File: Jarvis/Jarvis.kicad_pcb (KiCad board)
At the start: 2 copper layers, 34 x 65 mm, 121 parts, among them IC1 ADP1607, IC2 STM32F411CxUx, IC3 Si4460, IC4 MS5611-01BA03, IC5 MAX-8Q, IC6 MPU-9250, J1 PWR, J2 PYRO, J3 ARM, J4 EXT, P1 SWD_TC, P2 SMA, Q1 NFET, Q2 NFET, Q3 NFET, Q4 PFET, Q5 PFET, Q6 NFET, Q7 PFET, U1 MICROSD, Y1 26MHz, Y2 30MHz

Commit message: Schematic Complete
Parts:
- removed C22, C27, C30: 100nF, agg:0402-L
- removed C25: 1uF, agg:0603-L
- removed C33: 10nF, agg:0402-L
- removed J4: EXT, agg:SIL-254P-04
- removed R37: 1k, agg:0402-L
- removed REF**: Molex_PicoBlade_53261-0471, Connectors_Molex:Molex_PicoBlade_53261-0471
- added C19: 10nF, agg:0402-L, F.Cu at (241.0, 122.6)
- added C23: 100nF, agg:0402-L, F.Cu at (247.8, 116.4)
- added C26: 1uF, agg:0603-L, F.Cu at (217.8, 125.0)
- added C28: 100nF, agg:0402-L, F.Cu at (233.3, 130.3)
- added C29: 100nF, agg:0402-L, F.Cu at (218.4, 145.8)
- C11: value 8pF -> 100nF
- C13: value 100nF -> 8pF
- C14: value 4.7uF -> 100nF
- C15: value 10uF -> 4.7uF; footprint agg:0805 -> agg:0402-L
- C17: value 100nF -> 10uF; footprint agg:0402-L -> agg:0805
- IC2: value STM32F411CxUx -> MS5611-01BA03; footprint agg:QFN-48-EP-ST -> agg:MS5611
- IC3: value Si4460 -> STM32F411CxUx; footprint agg:QFN-20-EP-SI -> agg:QFN-48-EP-ST
- IC4: value MS5611-01BA03 -> Si4460; footprint agg:MS5611 -> agg:QFN-20-EP-SI; moved to F.Cu
- IC5: value MAX-8Q -> MPU-9250; footprint Library:MAX-7Q -> agg:QFN-24-MPU9250
- IC6: value MPU-9250 -> MAX-8Q; footprint agg:QFN-24-MPU9250 -> Library:MAX-7Q; moved to F.Cu
- J2: value PYRO -> ARM; footprint agg:S06B-PASK-2 -> agg:S03B-PASK-2
- J3: value ARM -> PYRO; footprint agg:S02B-PASK-2 -> agg:S06B-PASK-2
- LS1, U1: moved to F.Cu
- Q2: value NFET -> PFET
- Q4: value PFET -> NFET
- R1: value 47K -> 100R
- R10, R18, R19, R21: value 100R -> 10k
- R11, R22, R26: value 10k -> 1k
- R12, R13, R15, R20, R34: value 10k -> 100R
- R17: value 0R -> 10k; footprint agg:0603-L -> agg:0402-L
- R2: value 47K -> 243k; footprint agg:0402-L -> agg:0603-L
- R23, R24: value 10k -> 47K
- R25: value 100R -> 47K
- R27, R28: value 1k -> 47K
- R3: value 47K -> 330k; footprint agg:0402-L -> agg:0603-L
- R33, R9: value 1k -> 10k
- R35: value 100R -> 1k
- R4, R5: value 47K -> 10k
- R6: value 100R -> 0R; footprint agg:0402-L -> agg:0603-L
- R7: value 243k -> 100R; footprint agg:0603-L -> agg:0402-L
- R8: value 330k -> 10k; footprint agg:0603-L -> agg:0402-L
- moved IC5 116.4 mm to (160.3, 147.0), turned to 0 degrees
- moved Q6 107.3 mm to (199.0, 127.5), turned to 0 degrees
- moved Q4 97.0 mm to (171.7, 146.8), turned to 0 degrees
- moved IC3 95.0 mm to (173.7, 126.9)
- moved P1 89.6 mm to (165.4, 155.5), turned to 0 degrees
- moved U1 83.8 mm to (158.2, 116.5), turned to 0 degrees
- moved IC2 81.3 mm to (183.0, 110.1)
- moved C16 80.6 mm to (212.1, 116.1)
- moved D2 70.5 mm to (158.9, 161.0)
- moved D1 67.8 mm to (152.3, 160.5)
- moved P2 66.8 mm to (66.0, 73.0)
- moved R13 66.5 mm to (196.9, 158.8)
- moved C4 65.5 mm to (237.1, 114.5)
- moved LS1 64.4 mm to (186.4, 120.8), turned to 0 degrees
- moved D3 64.3 mm to (165.4, 160.8)
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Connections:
- C11 pad 1: GND -> 3v3
- C11 pad 2: Net-(C11-Pad2) -> GND
- C13 pad 1: 3v3 -> GND
- C13 pad 2: GND -> Net-(C13-Pad2)
- C14 pad 1: GND -> 3v3
- C14 pad 2: Net-(C14-Pad2) -> GND
- C15 pad 1: VBATT -> GND
- C15 pad 2: GND -> Net-(C15-Pad2)
- C16 pad 1: 3v3 -> VBATT
- C34 pad 1: Net-(C34-Pad1) -> /PYRO1_S
- C35 pad 1: /PYRO1_S -> /PYRO2_S
- C36 pad 1: /PYRO2_S -> /PYRO3_S
- C37 pad 1: /PYRO3_S -> 3v3
- IC2 pad 2: /STAT_EX_HBT -> 3v3
- IC2 pad 3: /STAT_HBT -> GND
- IC2 pad 4: /STAT_WRN -> GND
- IC2 pad 5: Net-(C11-Pad2) -> GND
- IC2 pad 7: /~RST -> /I2C1_SDA
- IC2 pad 8: GND -> /I2C1_SCL
- IC3 pad 1: GND -> 3v3
- IC3 pad 10: Net-(IC3-Pad10) -> /BEEPER
- IC3 pad 11: /nIRQ -> /SPI4_MOSI
- IC3 pad 12: /SPI4_SCK -> /USART2_TX
- IC3 pad 13: /SPI4_MISO -> /USART2_RX
- IC3 pad 14: /SPI4_MOSI -> /PYRO1_S
- IC3 pad 15: /SPI4_NSS1 -> /PYRO2_S
- IC3 pad 16: Net-(IC3-Pad16) -> /SDIO_CMD
- IC3 pad 17: Net-(IC3-Pad17) -> /PYRO3_S
- IC3 pad 18: GND -> /SPI5_SCK
- IC3 pad 19: Net-(IC3-Pad19) -> /SPI5_NSS1
- IC3 pad 2: Net-(C19-Pad2) -> /STAT_EX_HBT
- IC3 pad 20: Net-(IC3-Pad20) -> /GPS_RST
- IC3 pad 3: Net-(C20-Pad1) -> /STAT_HBT
- IC3 pad 4: Net-(C21-Pad1) -> /STAT_WRN
- IC3 pad 5: GND -> Net-(C12-Pad2)
- IC3 pad 6: 3v3 -> Net-(IC3-Pad6)
- IC3 pad 7: Net-(IC3-Pad7) -> /~RST
- IC3 pad 8: 3v3 -> GND
- IC3 pad 9: Net-(IC3-Pad9) -> 3v3
- IC4 pad 1: 3v3 -> GND
- IC4 pad 2: 3v3 -> Net-(C20-Pad2)
- IC4 pad 3: GND -> Net-(C21-Pad1)
- IC4 pad 4: GND -> Net-(C22-Pad1)
- IC4 pad 6: Net-(IC4-Pad6) -> 3v3
- IC4 pad 7: /I2C1_SDA -> Net-(IC4-Pad7)
- IC4 pad 8: /I2C1_SCL -> 3v3
- IC5 pad 1: GND -> 3v3
- IC5 pad 10: GND -> Net-(C29-Pad1)
- IC5 pad 11: Net-(AE1-Pad1) -> GND
- IC5 pad 12: GND -> /MPU_IRQ
- IC5 pad 13: Net-(IC5-Pad13) -> 3v3
- IC5 pad 18: Net-(IC5-Pad18) -> GND
- IC5 pad 2: Net-(FB1-Pad2) -> Net-(IC5-Pad2)
- IC5 pad 3: Net-(FB2-Pad2) -> Net-(IC5-Pad3)
- IC5 pad 6: 3v3 -> Net-(IC5-Pad6)
- IC5 pad 7: 3v3 -> Net-(IC5-Pad7)
- IC5 pad 9: /GPS_RST -> /SPI5_MISO
- IC6 pad 1: 3v3 -> GND
- IC6 pad 10: Net-(C34-Pad1) -> GND
- IC6 pad 11: GND -> Net-(AE1-Pad1)
- IC6 pad 12: /MPU_IRQ -> GND
- IC6 pad 13: 3v3 -> Net-(IC6-Pad13)
- IC6 pad 18: GND -> Net-(IC6-Pad18)
- IC6 pad 2: Net-(IC6-Pad2) -> Net-(FB1-Pad2)
- IC6 pad 3: Net-(IC6-Pad3) -> Net-(FB2-Pad2)
- IC6 pad 6: Net-(IC6-Pad6) -> 3v3
- IC6 pad 7: Net-(IC6-Pad7) -> 3v3
- IC6 pad 9: /SPI5_MISO -> /GPS_RST
- J2 pad 1: /PYRO1 -> VBATT
- J2 pad 2: GND -> /PYRO_SO
- J2 pad 3: /PYRO2 -> Net-(J2-Pad3)
- J3 pad 1: VBATT -> /PYRO1
- J3 pad 2: /PYRO_SO -> GND
- L2 pad 1: Net-(C20-Pad1) -> Net-(C21-Pad1)
- L2 pad 2: Net-(C19-Pad2) -> Net-(C20-Pad2)
- L3 pad 1: Net-(C21-Pad1) -> Net-(C22-Pad1)
- L7 pad 2: Net-(C28-Pad1) -> Net-(C30-Pad1)
- Q2 pad 2: GND -> /PYRO_SO
- Q2 pad 3: Net-(Q2-Pad3) -> /PYRO1
- Q4 pad 2: /PYRO_SO -> GND
- Q4 pad 3: /PYRO2 -> Net-(Q4-Pad3)
- Q5 pad 3: /PYRO1 -> /PYRO2
- R1 pad 1: /SDIO_D0 -> Net-(C13-Pad2)
- R1 pad 2: 3v3 -> Net-(IC3-Pad6)
- R10 pad 1: /PYRO1_F -> 3v3
- R10 pad 2: Net-(Q2-Pad1) -> /PYRO1
- R11 pad 1: /PYRO1_S -> Net-(J2-Pad3)
- R11 pad 2: /PYRO1 -> GND
- R12 pad 1: Net-(Q2-Pad1) -> Net-(Q1-Pad3)
- R12 pad 2: GND -> Net-(Q2-Pad1)
- R13 pad 1: 3v3 -> /BEEPER
- R13 pad 2: /I2C1_SCL -> Net-(Q3-Pad1)
- R14 pad 1: 3v3 -> /PYRO_SO
- R14 pad 2: /PYRO1 -> Net-(Q2-Pad1)
- R15 pad 1: 3v3 -> Net-(LS1-Pad2)
- R15 pad 2: /I2C1_SDA -> Net-(Q3-Pad3)
- R16 pad 1: Net-(Q2-Pad3) -> /PYRO2_F
- R16 pad 2: Net-(Q5-Pad1) -> Net-(Q4-Pad1)
- R17 pad 1: Net-(C28-Pad1) -> /PYRO2_S
- R17 pad 2: Net-(P2-Pad1) -> /PYRO2
- R18 pad 1: /BEEPER -> Net-(Q4-Pad1)
- R18 pad 2: Net-(Q1-Pad1) -> GND
- R19 pad 1: Net-(LS1-Pad2) -> 3v3
- R19 pad 2: Net-(Q1-Pad3) -> /PYRO2
- R2 pad 1: /SDIO_D1 -> Net-(IC1-Pad3)
- R2 pad 2: 3v3 -> GND
- R20 pad 1: /PYRO_SO -> Net-(Q4-Pad3)
- R21 pad 1: /PYRO2_F -> /PYRO_SO
- R21 pad 2: Net-(Q3-Pad1) -> Net-(Q5-Pad1)
- R22 pad 1: /PYRO2_S -> 3v3
- R22 pad 2: /PYRO2 -> Net-(D1-Pad2)
- R23 pad 1: Net-(Q3-Pad1) -> /SDIO_D0
- R23 pad 2: GND -> 3v3
- R24 pad 1: 3v3 -> /SDIO_D1
- R24 pad 2: /PYRO2 -> 3v3
- R25 pad 1: Net-(Q3-Pad3) -> /SDIO_D2
- R25 pad 2: Net-(Q4-Pad1) -> 3v3
- R26 pad 1: /PYRO_SO -> VBATT
- R26 pad 2: Net-(Q4-Pad1) -> Net-(D2-Pad2)
- R27 pad 1: VBATT -> /SDIO_D3
- R27 pad 2: Net-(D2-Pad2) -> 3v3
- R28 pad 1: /STAT_HBT -> /SDIO_CMD
- R28 pad 2: Net-(D3-Pad2) -> 3v3
- R29 pad 1: /STAT_WRN -> /STAT_HBT
- R29 pad 2: Net-(D4-Pad2) -> Net-(D3-Pad2)
- R3 pad 1: /SDIO_D2 -> Net-(IC1-Pad3)
- R33 pad 1: /STAT_EX_HBT -> 3v3
- R33 pad 2: Net-(J4-Pad1) -> /PYRO3
- R34 pad 1: 3v3 -> Net-(Q6-Pad3)
- R34 pad 2: /PYRO3 -> Net-(Q7-Pad1)
- R35 pad 1: Net-(Q6-Pad3) -> /STAT_WRN
- R35 pad 2: Net-(Q7-Pad1) -> Net-(D4-Pad2)
- R4 pad 1: /SDIO_D3 -> 3v3
- R4 pad 2: 3v3 -> /I2C1_SCL
- R5 pad 1: /SDIO_CMD -> 3v3
- R5 pad 2: 3v3 -> /I2C1_SDA
- R6 pad 1: Net-(C12-Pad2) -> Net-(C30-Pad1)
- R6 pad 2: Net-(IC2-Pad6) -> Net-(P2-Pad1)
- R7 pad 1: Net-(IC1-Pad3) -> /PYRO1_F
- R7 pad 2: GND -> Net-(Q1-Pad1)
- R8 pad 1: Net-(IC1-Pad3) -> /PYRO1_S
- R8 pad 2: 3v3 -> /PYRO1
- R9 pad 1: 3v3 -> Net-(Q1-Pad1)
- R9 pad 2: Net-(D1-Pad2) -> GND
- Y1 pad 1: Net-(C12-Pad2) -> Net-(C13-Pad2)
- Y1 pad 2: Net-(C11-Pad2) -> Net-(C12-Pad2)
- Y2 pad 1: Net-(IC3-Pad16) -> Net-(IC4-Pad16)
- Y2 pad 3: Net-(IC3-Pad17) -> Net-(IC4-Pad17)
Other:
- board size 34 x 65 mm -> 30 x 51 mm

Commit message: Added Testpoints
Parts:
- IC3, U1: moved to B.Cu

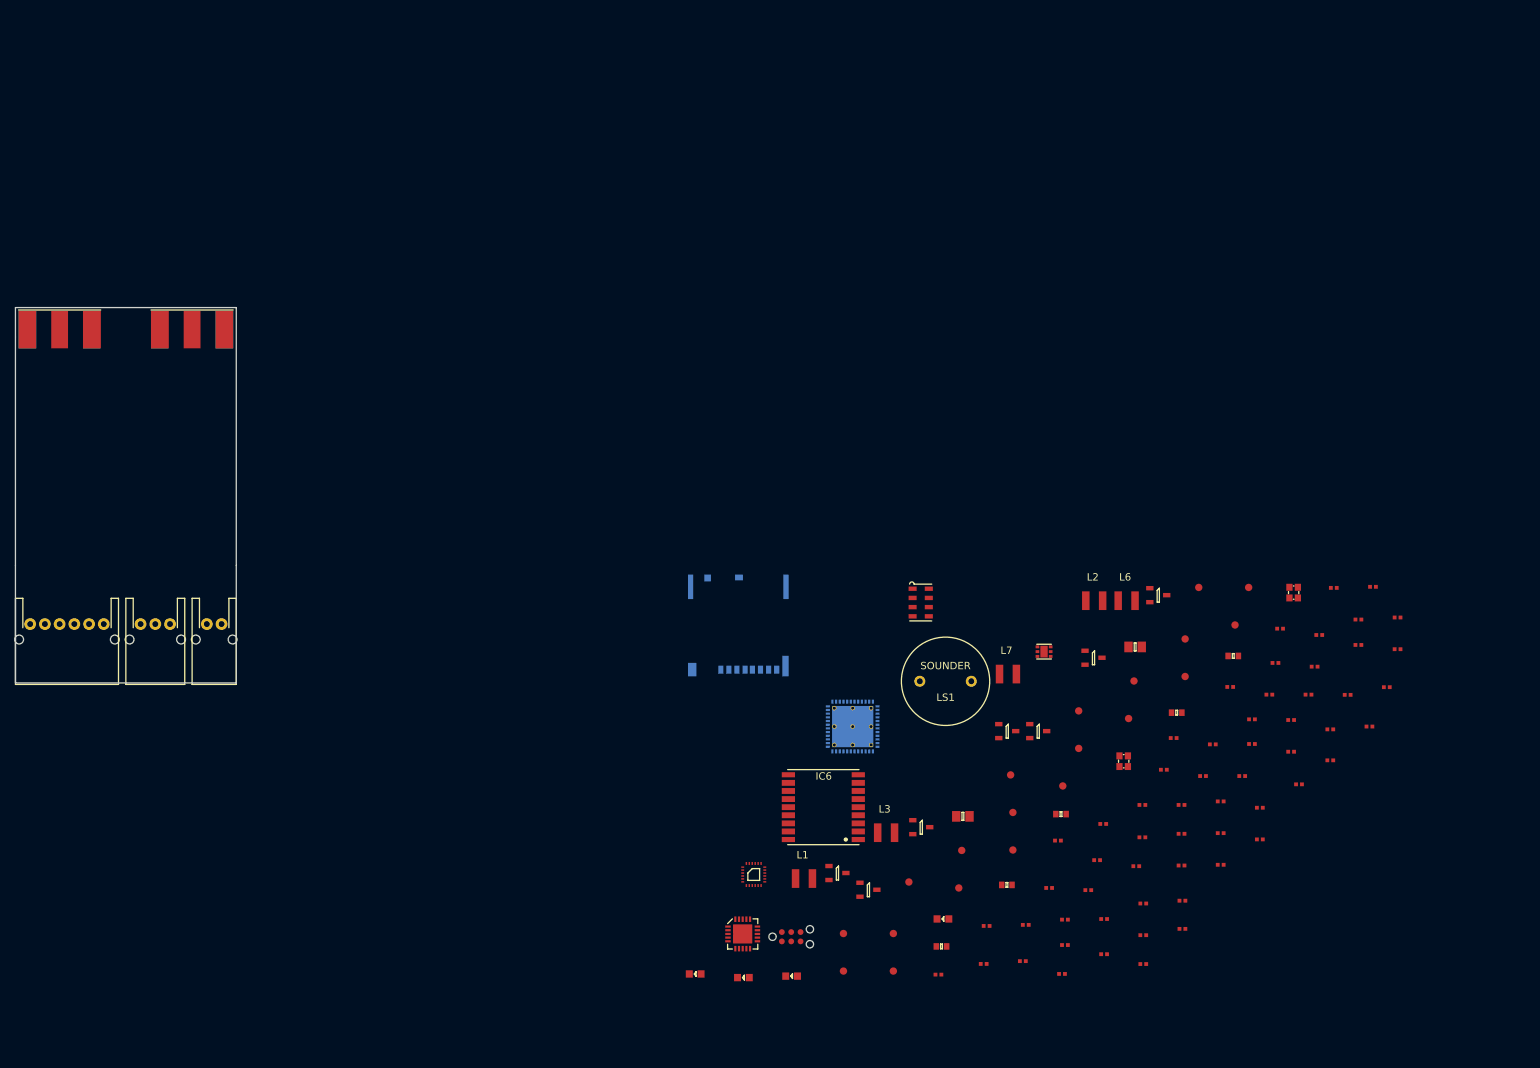
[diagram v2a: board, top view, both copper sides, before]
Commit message: Added mounts & placed ecternal connectors
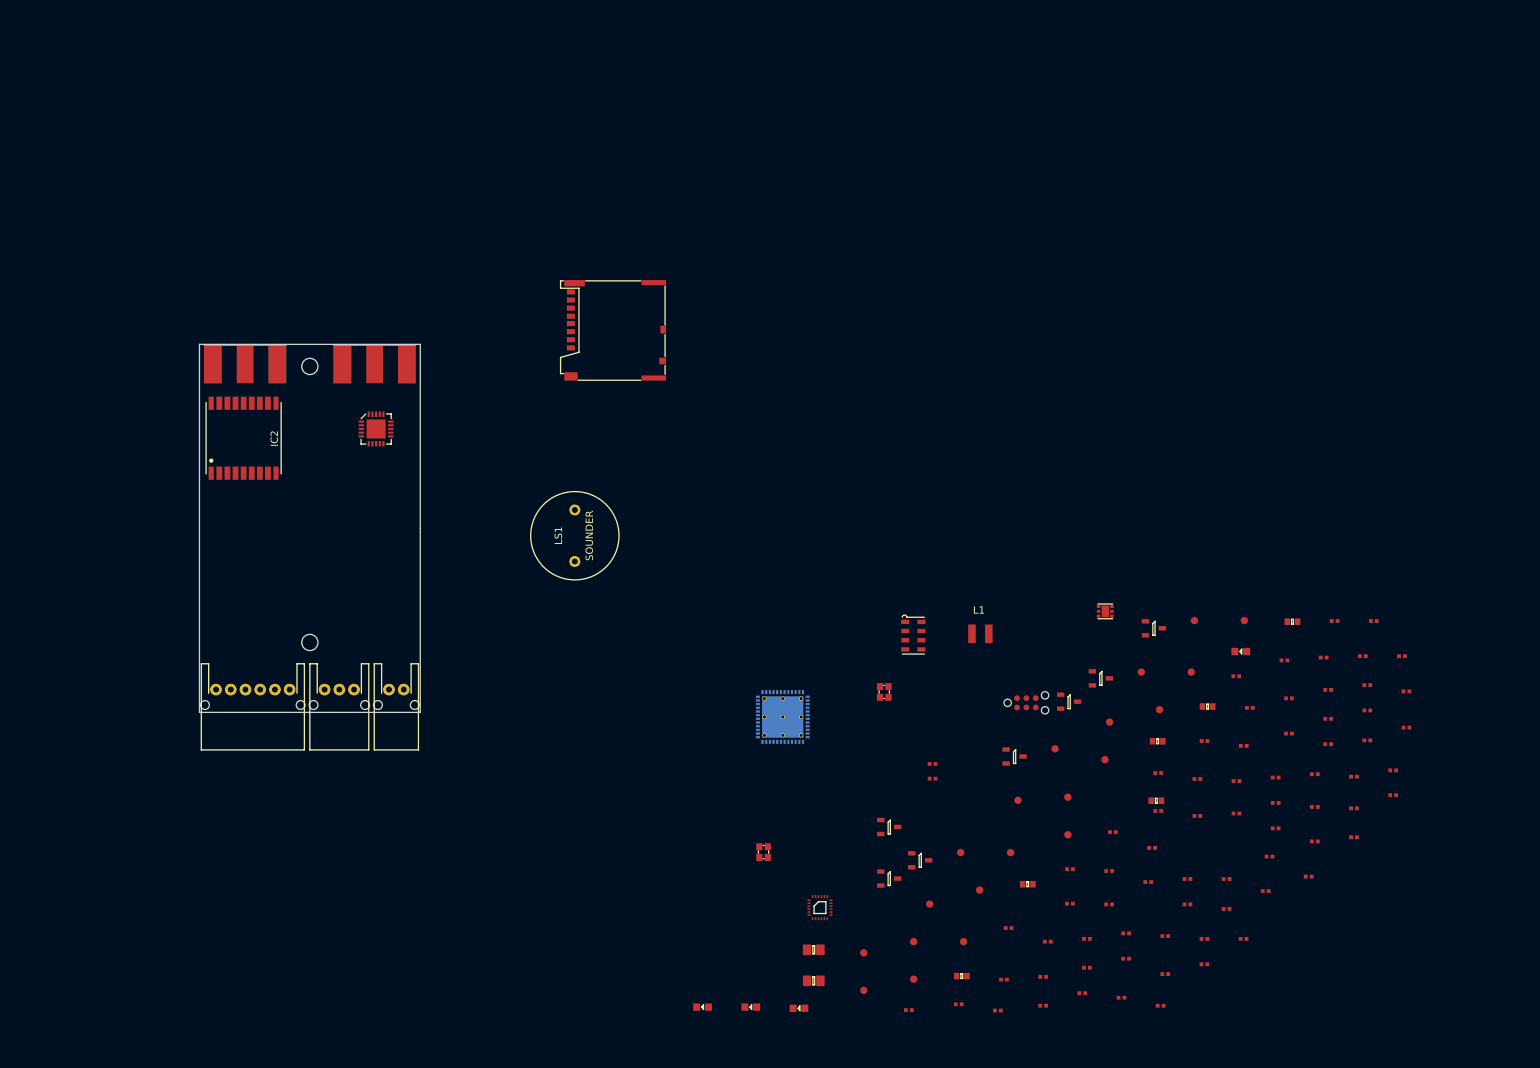
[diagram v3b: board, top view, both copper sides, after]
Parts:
- removed AE1: ANT, Library:SMA-142-0701-801
- added C20: 100nF, agg:0402-L, F.Cu at (216.2, 155.4)
- added C21: 8pF, agg:0402-L, F.Cu at (224.5, 147.6)
- added C22: 8pF, agg:0402-L, F.Cu at (231.2, 140.8)
- added C24: 2.7pF, agg:0402-L, F.Cu at (210.3, 163.8)
- added C25: 18pF, agg:0402-L, F.Cu at (236.5, 137.8)
- added C27: 15pF, agg:0402-L, F.Cu at (230.4, 144.6)
- added C30: 100nF, agg:0402-L, F.Cu at (249.0, 122.1)
- added C31: 100nF, agg:0402-L, F.Cu at (236.5, 142.5)
- added C33: 1uF, agg:0603-L, F.Cu at (215.2, 128.9)
- added L4: 18nH, agg:0402-L, F.Cu at (205.6, 155.8)
- added L5: 18nH, agg:0402-L, F.Cu at (199.6, 160.9)
- added P3: SWD_TC, agg:TC2030-NL, F.Cu at (197.3, 123.7)
- added REF**: MountingHole_2.2mm_M2_ISO14580, Mounting_Holes:MountingHole_2.2mm_M2_ISO14580, F.Cu at (100.0, 78.0)
- added REF**: MountingHole_2.2mm_M2_ISO14580, Mounting_Holes:MountingHole_2.2mm_M2_ISO14580, F.Cu at (100.0, 115.5)
- C1, C15: value 4.7uF -> 100nF
- C11: value 100nF -> 10nF
- C12, C13: value 8pF -> 100nF
- C16: value 10uF -> 1uF; footprint agg:0805 -> agg:0603-L
- C17: value 10uF -> 100nF; footprint agg:0805 -> agg:0402-L
- C19: value 10nF -> 4.7uF
- C2: value 100nF -> 10uF; footprint agg:0402-L -> agg:0805
- C23: value 100nF -> 5.1pF
- C26: value 1uF -> 8.2pF; footprint agg:0603-L -> agg:0402-L
- C28: value 100nF -> 8.2pF
- C3: value 1uF -> 10uF; footprint agg:0603-L -> agg:0805
- C32: value 100nF -> 2.2uF; footprint agg:0402-L -> agg:0603-L
- C35: value 100nF -> 100pF
- C36: value 100nF -> 220pF
- C7: value 100nF -> 4.7uF
- IC2: value MS5611-01BA03 -> MAX-8Q; footprint agg:MS5611 -> Library:MAX-7Q
- IC3: value STM32F411CxUx -> MPU-9250; footprint agg:QFN-48-EP-ST -> agg:QFN-24-MPU9250; moved to F.Cu
- IC4: value Si4460 -> STM32F411CxUx; footprint agg:QFN-20-EP-SI -> agg:QFN-48-EP-ST; moved to B.Cu
- IC5: value MPU-9250 -> Si4460; footprint agg:QFN-24-MPU9250 -> agg:QFN-20-EP-SI
- IC6: value MAX-8Q -> MS5611-01BA03; footprint Library:MAX-7Q -> agg:MS5611
- J1: value PWR -> PYRO; footprint agg:S02B-PASK-2 -> agg:S06B-PASK-2
- J2: value ARM -> PWR; footprint agg:S03B-PASK-2 -> agg:S02B-PASK-2
- J3: value PYRO -> ARM; footprint agg:S06B-PASK-2 -> agg:S03B-PASK-2
- L2: footprint Inductors_NEOSID:Neosid_Inductor_SM-NE29_SMD1008 -> agg:0402-L
- L3: value 220nH -> 56nH; footprint Inductors_NEOSID:Neosid_Inductor_SM-NE29_SMD1008 -> agg:0402-L
- L6: value 18nH -> 56nH; footprint Inductors_NEOSID:Neosid_Inductor_SM-NE29_SMD1008 -> agg:0402-L
- L7: value 18nH -> 220nH; footprint Inductors_NEOSID:Neosid_Inductor_SM-NE29_SMD1008 -> agg:0603-L
- P1: value SWD_TC -> SMA; footprint agg:TC2030-NL -> Library:SMA-142-0701-801
- Q1, Q3: value NFET -> PFET
- Q5, Q7: value PFET -> NFET
- R1, R12, R13, R15, R16, R20: value 100R -> 10k
- R10, R33, R4, R5, R8, R9: value 10k -> 100R
- R11: value 1k -> 243k; footprint agg:0402-L -> agg:0603-L
- R2: value 243k -> 10k; footprint agg:0603-L -> agg:0402-L
- R21: value 10k -> 1k
- R23, R24, R25: value 47K -> 1k
- R26: value 1k -> 100R
- R29: value 1k -> 47K
- R3: value 330k -> 10k; footprint agg:0603-L -> agg:0402-L
- R30: value 100R -> 47K
- R31: value 10k -> 47K
- R32: value 10k -> 0R
- R35: value 1k -> 10k
- R6: value 0R -> 100R; footprint agg:0603-L -> agg:0402-L
- R7: value 100R -> 330k; footprint agg:0402-L -> agg:0603-L
- U1: moved to F.Cu
- moved P1 107.5 mm to (91.2, 77.8)
- moved IC2 91.7 mm to (95.4, 83.0), turned to 270 degrees
- moved D1 86.1 mm to (226.5, 116.7)
- moved IC5 79.3 mm to (109.0, 86.5)
- moved R24 73.0 mm to (188.2, 164.7)
- moved C3 72.1 mm to (168.5, 161.5)
- moved L3 69.1 mm to (243.1, 117.4)
- moved TP10 62.3 mm to (219.7, 119.5)
- moved C2 61.0 mm to (168.5, 157.3)
- moved C4 58.0 mm to (194.9, 154.3)
- moved Y2 57.2 mm to (178.0, 122.2)
- moved R11 56.6 mm to (188.6, 160.8)
- moved R16 54.8 mm to (243.7, 124.7)
- moved C14 54.2 mm to (232.4, 117.9)
- moved LS1 54.1 mm to (136.0, 101.0), turned to 270 degrees
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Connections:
- net /STAT_EX_HBT renamed Net-(IC3-Pad2)
- C12 pad 1: GND -> 3v3
- C12 pad 2: Net-(C12-Pad2) -> GND
- C13 pad 1: GND -> 3v3
- C13 pad 2: Net-(C13-Pad2) -> GND
- C15 pad 1: GND -> Net-(C15-Pad1)
- C15 pad 2: Net-(C15-Pad2) -> GND
- C16 pad 1: VBATT -> 3v3
- C19 pad 1: 3v3 -> GND
- C19 pad 2: GND -> Net-(C19-Pad2)
- C2 pad 1: 3v3 -> VBATT
- C23 pad 1: 3v3 -> GND
- C23 pad 2: GND -> Net-(C23-Pad2)
- C26 pad 1: 3v3 -> Net-(C24-Pad2)
- C28 pad 1: 3v3 -> Net-(C28-Pad1)
- C29 pad 1: Net-(C29-Pad1) -> 3v3
- C34 pad 1: /PYRO1_S -> 3v3
- C35 pad 1: /PYRO2_S -> 3v3
- C36 pad 1: /PYRO3_S -> 3v3
- C4 pad 1: 3v3 -> /PYRO1_S
- C5 pad 1: 3v3 -> /PYRO2_S
- C6 pad 1: 3v3 -> /PYRO3_S
- C7 pad 1: /~RST -> 3v3
- IC2 pad 1: 3v3 -> GND
- IC2 pad 2: 3v3 -> Net-(FB1-Pad2)
- IC2 pad 3: GND -> Net-(FB2-Pad2)
- IC2 pad 4: GND -> Net-(IC2-Pad4)
- IC2 pad 5: GND -> Net-(IC2-Pad5)
- IC2 pad 6: Net-(IC2-Pad6) -> 3v3
- IC2 pad 7: /I2C1_SDA -> 3v3
- IC2 pad 8: /I2C1_SCL -> 3v3
- IC3 pad 10: /BEEPER -> Net-(C15-Pad1)
- IC3 pad 11: /SPI4_MOSI -> GND
- IC3 pad 12: /USART2_TX -> /MPU_IRQ
- IC3 pad 13: /USART2_RX -> 3v3
- IC3 pad 14: /PYRO1_S -> Net-(IC3-Pad14)
- IC3 pad 15: /PYRO2_S -> Net-(IC3-Pad15)
- IC3 pad 16: /SDIO_CMD -> Net-(IC3-Pad16)
- IC3 pad 17: /PYRO3_S -> Net-(IC3-Pad17)
- IC3 pad 18: /SPI5_SCK -> GND
- IC3 pad 19: /SPI5_NSS1 -> Net-(IC3-Pad19)
- IC3 pad 20: /GPS_RST -> GND
- IC3 pad 21: /nIRQ -> Net-(IC3-Pad21)
- IC3 pad 22: Net-(C15-Pad2) -> /SPI5_NSS1
- IC3 pad 23: GND -> /SPI5_SCK
- IC3 pad 24: 3v3 -> /SPI5_MOSI
- IC3 pad 3: /STAT_HBT -> Net-(IC3-Pad3)
- IC3 pad 4: /STAT_WRN -> Net-(IC3-Pad4)
- IC3 pad 5: Net-(C12-Pad2) -> Net-(IC3-Pad5)
- IC3 pad 7: /~RST -> Net-(IC3-Pad7)
- IC3 pad 8: GND -> 3v3
- IC3 pad 9: 3v3 -> /SPI5_MISO
- IC4 pad 1: GND -> 3v3
- IC4 pad 10: Net-(IC4-Pad10) -> /BEEPER
- IC4 pad 11: /nIRQ -> /SPI4_MOSI
- IC4 pad 12: /SPI4_SCK -> /USART2_TX
- IC4 pad 13: /SPI4_MISO -> /USART2_RX
- IC4 pad 14: /SPI4_MOSI -> /PYRO1_S
- IC4 pad 15: /SPI4_NSS1 -> /PYRO2_S
- IC4 pad 16: Net-(IC4-Pad16) -> /SDIO_CMD
- IC4 pad 17: Net-(IC4-Pad17) -> /PYRO3_S
- IC4 pad 18: GND -> /SPI5_SCK
- IC4 pad 19: Net-(IC4-Pad19) -> /SPI5_NSS1
- IC4 pad 2: Net-(C20-Pad2) -> /STAT_WRN
- IC4 pad 20: Net-(IC4-Pad20) -> /GPS_RST
- IC4 pad 3: Net-(C21-Pad1) -> /STAT_HBT
- IC4 pad 4: Net-(C22-Pad1) -> Net-(IC4-Pad4)
- IC4 pad 5: GND -> Net-(C21-Pad2)
- IC4 pad 6: 3v3 -> Net-(IC4-Pad6)
- IC4 pad 7: Net-(IC4-Pad7) -> /~RST
- IC4 pad 8: 3v3 -> GND
- IC4 pad 9: Net-(IC4-Pad9) -> 3v3
- IC5 pad 1: 3v3 -> GND
- IC5 pad 10: Net-(C29-Pad1) -> Net-(IC5-Pad10)
- IC5 pad 11: GND -> /nIRQ
- IC5 pad 12: /MPU_IRQ -> /SPI4_SCK
- IC5 pad 13: 3v3 -> /SPI4_MISO
- IC5 pad 14: Net-(IC5-Pad14) -> /SPI4_MOSI
- IC5 pad 15: Net-(IC5-Pad15) -> /SPI4_NSS1
- IC5 pad 2: Net-(IC5-Pad2) -> Net-(C23-Pad2)
- IC5 pad 20: GND -> Net-(IC5-Pad20)
- IC5 pad 3: Net-(IC5-Pad3) -> Net-(C24-Pad1)
- IC5 pad 4: Net-(IC5-Pad4) -> Net-(C25-Pad1)
- IC5 pad 5: Net-(IC5-Pad5) -> GND
- IC5 pad 6: Net-(IC5-Pad6) -> 3v3
- IC5 pad 9: /SPI5_MISO -> Net-(IC5-Pad9)
- IC6 pad 1: GND -> 3v3
- IC6 pad 2: Net-(FB1-Pad2) -> 3v3
- IC6 pad 3: Net-(FB2-Pad2) -> GND
- IC6 pad 4: Net-(IC6-Pad4) -> GND
- IC6 pad 5: Net-(IC6-Pad5) -> GND
- IC6 pad 6: 3v3 -> Net-(IC6-Pad6)
- IC6 pad 7: 3v3 -> /I2C1_SDA
- IC6 pad 8: 3v3 -> /I2C1_SCL
- J1 pad 1: VBATT -> /PYRO1
- J2 pad 2: /PYRO_SO -> GND
- J3 pad 1: /PYRO1 -> VBATT
- J3 pad 2: GND -> /PYRO_SO
- J3 pad 3: /PYRO2 -> Net-(J3-Pad3)
- L2 pad 1: Net-(C21-Pad1) -> Net-(C24-Pad1)
- L2 pad 2: Net-(C20-Pad2) -> Net-(C23-Pad2)
- L3 pad 1: Net-(C22-Pad1) -> Net-(C23-Pad2)
- L3 pad 2: 3v3 -> Net-(C24-Pad2)
- L6 pad 2: Net-(C27-Pad1) -> Net-(C24-Pad2)
- L7 pad 1: Net-(C27-Pad1) -> Net-(C25-Pad1)
- L7 pad 2: Net-(C30-Pad1) -> 3v3
- P1 pad 1: 3v3 -> Net-(IC2-Pad11)
- P1 pad 2: /SWDIO -> GND
- P1 pad 3: /~RST -> GND
- P1 pad 4: /SWCLK -> GND
- Q1 pad 2: GND -> /PYRO_SO
- Q1 pad 3: Net-(Q1-Pad3) -> /PYRO1
- Q2 pad 3: /PYRO1 -> /PYRO2
- Q3 pad 2: GND -> /PYRO_SO
- Q3 pad 3: Net-(Q3-Pad3) -> /PYRO3
- Q5 pad 2: /PYRO_SO -> GND
- Q5 pad 3: /PYRO2 -> Net-(Q5-Pad3)
- Q7 pad 2: /PYRO_SO -> GND
- Q7 pad 3: /PYRO3 -> Net-(Q7-Pad3)
- R1 pad 1: Net-(C13-Pad2) -> /PYRO_SO
- R1 pad 2: Net-(IC3-Pad6) -> Net-(Q1-Pad1)
- R10 pad 1: 3v3 -> /PYRO3_F
- R10 pad 2: /PYRO1 -> Net-(Q6-Pad1)
- R11 pad 1: Net-(J2-Pad3) -> Net-(IC1-Pad3)
- R12 pad 1: Net-(Q1-Pad3) -> Net-(Q4-Pad1)
- R12 pad 2: Net-(Q2-Pad1) -> GND
- R13 pad 1: /BEEPER -> Net-(Q5-Pad1)
- R13 pad 2: Net-(Q3-Pad1) -> GND
- R14 pad 1: /PYRO_SO -> Net-(Q6-Pad1)
- R14 pad 2: Net-(Q2-Pad1) -> GND
- R15 pad 1: Net-(LS1-Pad2) -> 3v3
- R15 pad 2: Net-(Q3-Pad3) -> /PYRO1
- R16 pad 1: /PYRO2_F -> 3v3
- R16 pad 2: Net-(Q4-Pad1) -> /PYRO2
- R17 pad 1: /PYRO2_S -> 3v3
- R17 pad 2: /PYRO2 -> /PYRO3
- R18 pad 1: Net-(Q4-Pad1) -> /PYRO1_S
- R18 pad 2: GND -> /PYRO1
- R19 pad 1: 3v3 -> /PYRO2_S
- R2 pad 1: Net-(IC1-Pad3) -> /PYRO_SO
- R2 pad 2: GND -> Net-(Q2-Pad1)
- R20 pad 1: Net-(Q4-Pad3) -> /PYRO3_S
- R20 pad 2: Net-(Q5-Pad1) -> /PYRO3
- R21 pad 1: /PYRO_SO -> 3v3
- R21 pad 2: Net-(Q5-Pad1) -> Net-(D1-Pad2)
- R22 pad 1: 3v3 -> VBATT
- R22 pad 2: Net-(D1-Pad2) -> Net-(D2-Pad2)
- R23 pad 1: /SDIO_D0 -> /STAT_HBT
- R23 pad 2: 3v3 -> Net-(D3-Pad2)
- R24 pad 1: /SDIO_D1 -> /STAT_WRN
- R24 pad 2: 3v3 -> Net-(D4-Pad2)
- R25 pad 1: /SDIO_D2 -> Net-(J3-Pad3)
- R25 pad 2: 3v3 -> GND
- R26 pad 1: VBATT -> Net-(C22-Pad2)
- R26 pad 2: Net-(D2-Pad2) -> Net-(IC4-Pad6)
- R27 pad 1: /SDIO_D3 -> /SDIO_D0
- R28 pad 1: /SDIO_CMD -> /SDIO_D1
- R29 pad 1: /STAT_HBT -> /SDIO_D2
- R29 pad 2: Net-(D3-Pad2) -> 3v3
- R3 pad 1: Net-(IC1-Pad3) -> /PYRO_SO
- R3 pad 2: 3v3 -> Net-(Q3-Pad1)
- R30 pad 1: /PYRO3_F -> /SDIO_D3
- R30 pad 2: Net-(Q6-Pad1) -> 3v3
- R31 pad 1: Net-(Q6-Pad1) -> /SDIO_CMD
- R31 pad 2: GND -> 3v3
- R32 pad 1: /PYRO3_S -> Net-(C28-Pad1)
- R32 pad 2: /PYRO3 -> Net-(P2-Pad1)
- R33 pad 1: 3v3 -> Net-(LS1-Pad2)
- R33 pad 2: /PYRO3 -> Net-(Q7-Pad3)
- R34 pad 1: Net-(Q6-Pad3) -> /BEEPER
- R35 pad 1: /STAT_WRN -> 3v3
- R35 pad 2: Net-(D4-Pad2) -> /I2C1_SCL
- R36 pad 1: /PYRO_SO -> 3v3
- R36 pad 2: Net-(Q7-Pad1) -> /I2C1_SDA
- R4 pad 1: 3v3 -> Net-(Q4-Pad3)
- R4 pad 2: /I2C1_SCL -> Net-(Q1-Pad1)
- R5 pad 1: 3v3 -> Net-(Q5-Pad3)
- R5 pad 2: /I2C1_SDA -> Net-(Q2-Pad1)
- R6 pad 1: Net-(C30-Pad1) -> Net-(Q6-Pad3)
- R6 pad 2: Net-(P2-Pad1) -> Net-(Q3-Pad1)
- R7 pad 1: /PYRO1_F -> Net-(IC1-Pad3)
- R7 pad 2: Net-(Q1-Pad1) -> 3v3
- R8 pad 1: /PYRO1_S -> /PYRO1_F
- R8 pad 2: /PYRO1 -> Net-(Q4-Pad1)
- R9 pad 1: Net-(Q1-Pad1) -> /PYRO2_F
- R9 pad 2: GND -> Net-(Q5-Pad1)
- TP1 pad 1: /SPI5_MOSI -> /BEEPER
- TP10 pad 1: /I2C1_SDA -> /SPI5_MISO
- TP11 pad 1: /nIRQ -> /SPI5_SCK
- TP12 pad 1: /SPI4_NSS1 -> /SPI5_NSS1
- TP13 pad 1: /SPI4_SCK -> /PYRO1_F
- TP14 pad 1: /BEEPER -> /PYRO2_F
- TP15 pad 1: /SPI4_MOSI -> /PYRO3_F
- TP16 pad 1: /USART2_TX -> /I2C1_SCL
- TP17 pad 1: /USART2_RX -> /I2C1_SDA
- TP18 pad 1: /PYRO1_S -> /nIRQ
- TP19 pad 1: /PYRO2_S -> /SPI4_NSS1
- TP2 pad 1: /SPI4_MISO -> /SPI4_MOSI
- TP20 pad 1: /PYRO3_S -> /SPI4_SCK
- TP3 pad 1: /SPI5_MISO -> /USART2_TX
- TP4 pad 1: /SPI5_SCK -> /USART2_RX
- TP5 pad 1: /SPI5_NSS1 -> /PYRO1_S
- TP6 pad 1: /PYRO1_F -> /PYRO2_S
- TP7 pad 1: /PYRO2_F -> /PYRO3_S
- TP8 pad 1: /PYRO3_F -> /SPI5_MOSI
- TP9 pad 1: /I2C1_SCL -> /SPI4_MISO
- Y1 pad 1: Net-(C13-Pad2) -> Net-(C21-Pad2)
- Y1 pad 2: Net-(C12-Pad2) -> GND
- Y1 pad 3: (no net) -> Net-(C22-Pad2)
- Y1 pad 4: (no net) -> GND
- Y2 pad 1: Net-(IC4-Pad16) -> Net-(IC5-Pad16)
- Y2 pad 3: Net-(IC4-Pad17) -> Net-(IC5-Pad17)
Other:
- board size 30 x 51 mm -> 30 x 50 mm
- net class Default: clearance 0.2 -> 0.127; trace_width 0.25 -> 0.22; via_drill 0.4 -> 0.3
- rule trace_clearance: 0.2 -> 0.127

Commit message: Started PCB layout
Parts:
- added D10: ESD_DIODE, agg:0402-L, F.Cu at (101.7, 135.8)
- added D5: ESD_DIODE, agg:0402-L, F.Cu at (103.0, 134.4)
- added D6: ESD_DIODE, agg:0402-L, F.Cu at (103.6, 135.9)
- added D7: ESD_DIODE, agg:0402-L, F.Cu at (96.2, 120.4)
- added D8: ESD_DIODE, agg:0402-L, F.Cu at (92.2, 120.4)
- added D9: ESD_DIODE, agg:0402-L, F.Cu at (88.2, 120.4)
- R25: moved to B.Cu
- moved R1 159.1 mm to (89.2, 117.0), turned to 270 degrees
- moved R4 153.0 mm to (85.5, 114.6), turned to 270 degrees
- moved R16 151.1 mm to (92.7, 119.6), turned to 180 degrees
- moved R15 143.7 mm to (88.7, 119.6), turned to 180 degrees
- moved R5 143.5 mm to (90.1, 114.6), turned to 270 degrees
- moved R17 142.0 mm to (96.7, 119.6), turned to 180 degrees
- moved R12 135.1 mm to (89.2, 114.2), turned to 270 degrees
- moved R6 132.7 mm to (94.7, 114.7), turned to 270 degrees
- moved R20 131.3 mm to (95.5, 119.2), turned to 270 degrees
- moved R19 130.9 mm to (91.5, 119.2), turned to 270 degrees
- moved R10 130.1 mm to (98.4, 112.7), turned to 270 degrees
- moved R8 129.6 mm to (89.2, 112.7), turned to 270 degrees
- moved R25 129.4 mm to (102.2, 123.7), turned to 270 degrees
- moved C5 128.8 mm to (92.7, 118.8)
- moved Q5 123.2 mm to (91.5, 112.9), turned to 180 degrees
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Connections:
- J3 pad 1: VBATT -> Net-(J3-Pad1)
- J3 pad 3: Net-(J3-Pad3) -> VBATT
- R25 pad 1: Net-(J3-Pad3) -> Net-(J3-Pad1)
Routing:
- net /PYRO_SO: track 0.00 -> 15.8 mm, vias 0 -> 3
- net /PYRO1: track 0.00 -> 10.1 mm
- net /PYRO3: track 0.00 -> 9.48 mm
- net /PYRO2: track 0.00 -> 9.20 mm
- net Net-(Q1-Pad1): track 0.00 -> 5.14 mm
- net Net-(Q3-Pad1): track 0.00 -> 4.86 mm
- net Net-(Q2-Pad1): track 0.00 -> 4.86 mm
- net VBATT: track 0.00 -> 4.75 mm
- net Net-(Q4-Pad1): track 0.00 -> 2.18 mm
- net Net-(Q5-Pad1): track 0.00 -> 1.96 mm
- net Net-(Q6-Pad1): track 0.00 -> 1.95 mm
- net Net-(Q4-Pad3): track 0.00 -> 1.66 mm
- net Net-(J3-Pad1): track 0.00 -> 1.50 mm
- net Net-(Q5-Pad3): track 0.00 -> 1.43 mm
- net /PYRO3_S: track 0.00 -> 0.80 mm
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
